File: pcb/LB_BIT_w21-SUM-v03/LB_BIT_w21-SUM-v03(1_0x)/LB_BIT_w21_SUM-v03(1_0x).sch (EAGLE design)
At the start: 24 parts

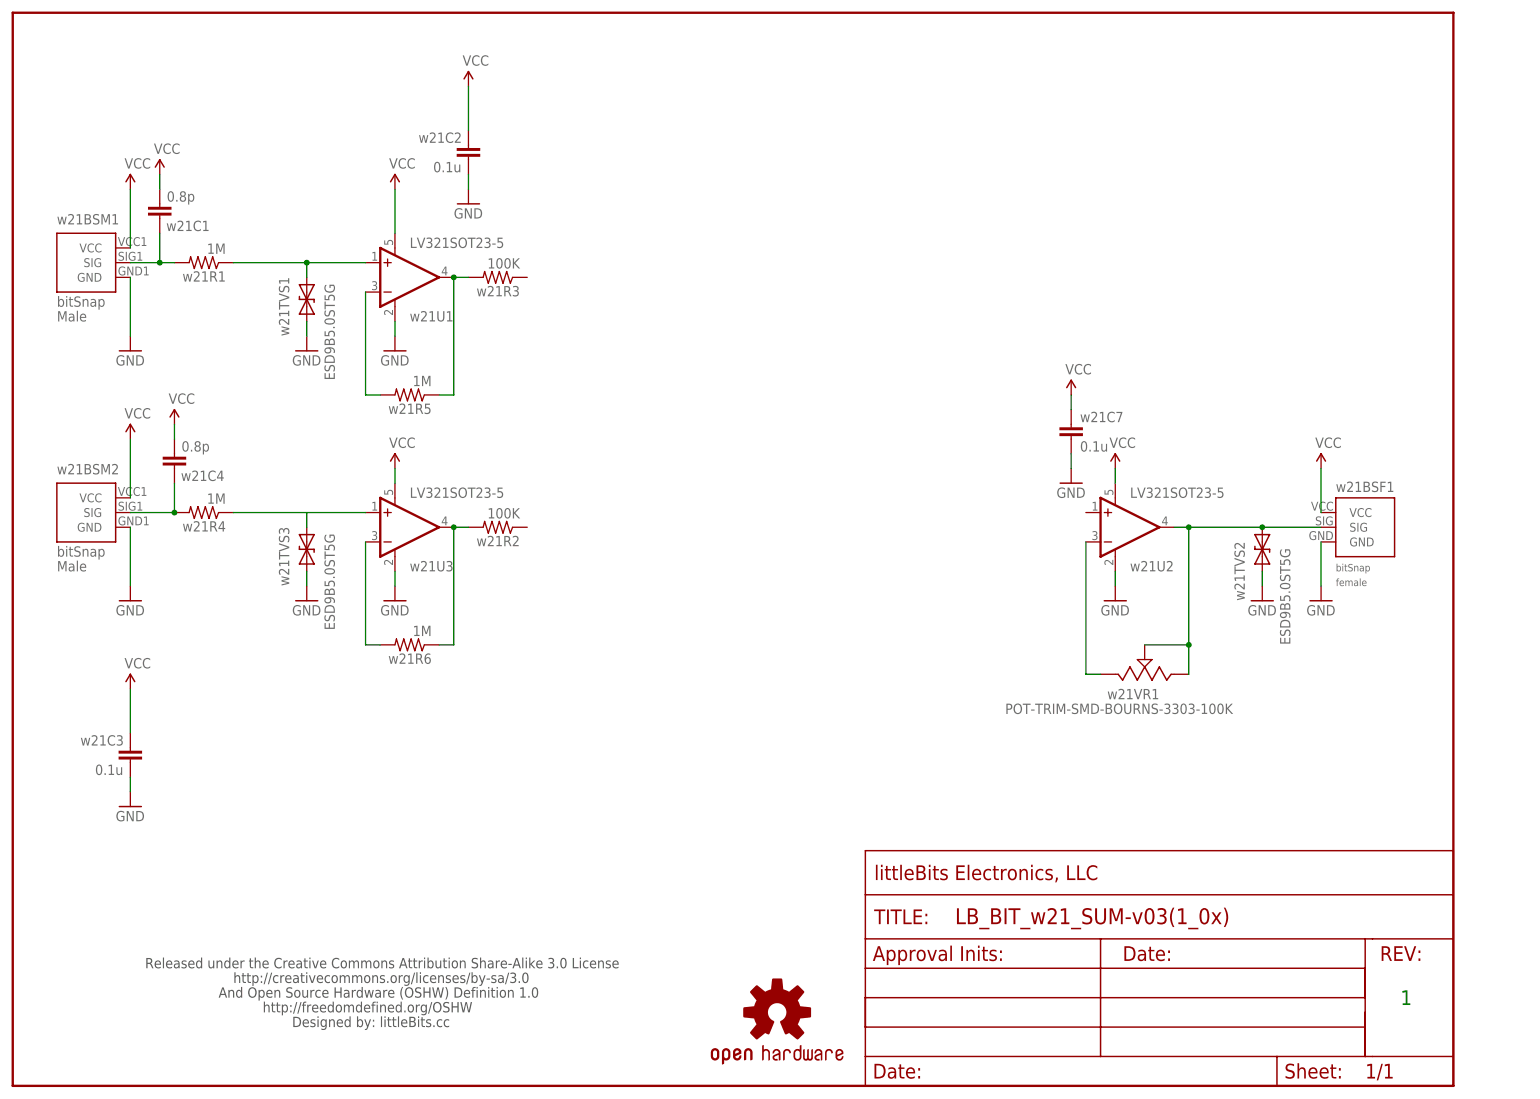
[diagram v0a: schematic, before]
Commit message: Tuned inputs and reference rail, though it may not be neccessary.  Sketched out the DC mixer and output buffer.
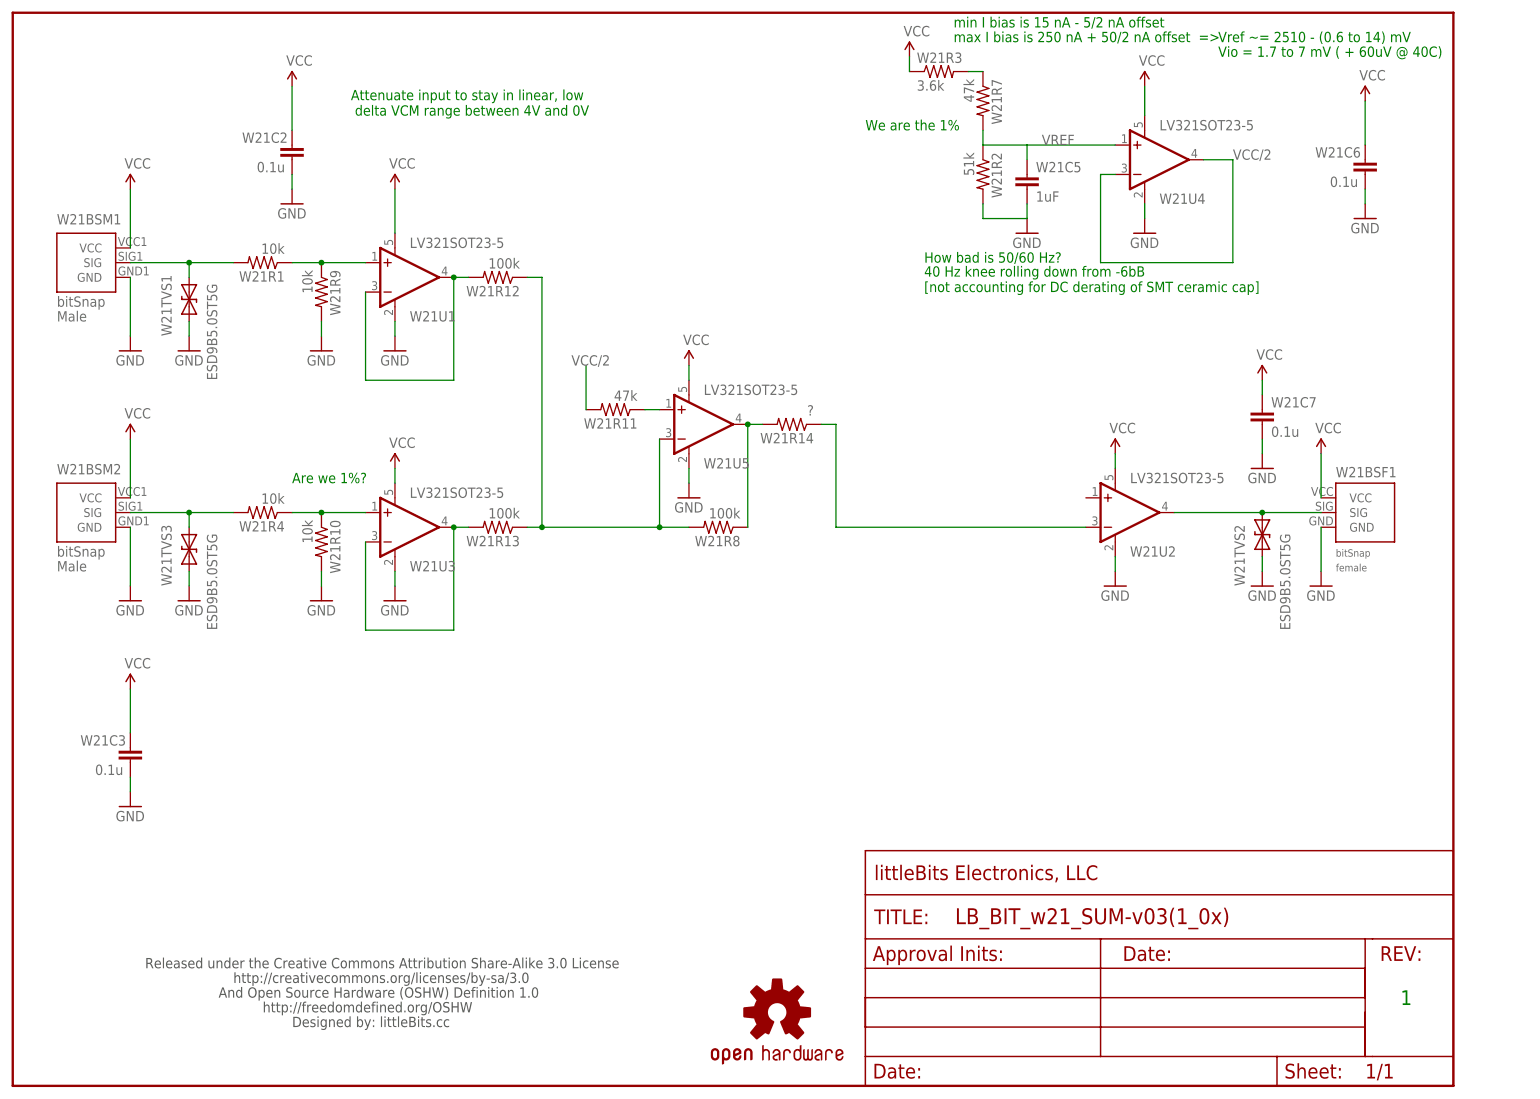
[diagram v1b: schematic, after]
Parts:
- removed w21BSF1: BITSNAP_V03_FEMALE, bitSnap:BITSNAP_V03_FEMALE
- removed w21C1, w21C4: 0.8p, LITTLEBITS:CAPCAP-0603
- removed w21C2, w21C7: 0.1u, LITTLEBITS:CAPCAP-0603
- removed w21R1, w21R4, w21R5, w21R6: 1M, LITTLEBITS:RESISTOR0603
- removed w21TVS1, w21TVS2, w21TVS3: ESD9B5.0ST5G, LITTLEBITS:DIODE-TVSSOD-923
- removed w21U2: LV321SOT23-5, LITTLEBITS:LV321SOT23-5
- removed w21VR1: POT-TRIM-SMD-BOURNS-3303-100K, LITTLEBITS:POT-TRIM-SMD-BOURNS-3303
- added W21BSF1: BITSNAP_V03_FEMALE, bitSnap:BITSNAP_V03_FEMALE
- added W21C2, W21C6, W21C7: 0.1u, LITTLEBITS:CAPCAP-0603
- added W21C5: 1uF, LITTLEBITS:CAPCAP-0603
- added W21R1, W21R10, W21R4, W21R9: 10k, LITTLEBITS:RESISTOR0603
- added W21R11, W21R7: 47k, LITTLEBITS:RESISTOR0603
- added W21R14: ?, LITTLEBITS:RESISTOR0603
- added W21R2: 51k, LITTLEBITS:RESISTOR0603
- added W21R3: 3.6k, LITTLEBITS:RESISTOR0603
- added W21R8: 100k, LITTLEBITS:RESISTOR0603
- added W21TVS1, W21TVS2, W21TVS3: ESD9B5.0ST5G, LITTLEBITS:DIODE-TVSSOD-923
- added W21U2, W21U4, W21U5: LV321SOT23-5, LITTLEBITS:LV321SOT23-5
- W21R12, W21R13: value 100K -> 100k
- renumbered w21BSM1 to W21BSM1, w21BSM2 to W21BSM2, w21C3 to W21C3, w21R2 to W21R13, w21R3 to W21R12, w21U1 to W21U1, w21U3 to W21U3
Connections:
- removed net N$4: W21R13.2, W21U3.OUT, w21R6.1
- removed net N$9: W21U1.-IN, w21R5.2
- new net N$1: W21R3.2, W21R7.1
- new net N$12: W21R12.1, W21R13.1, W21R8.2, W21U5.-IN
- new net N$13: W21R11.1, W21U5.+IN
- new net N$15: W21R14.1, W21U2.-IN
- new net VCC/2: W21R11.2, W21U4.-IN, W21U4.OUT
- new net VREF: W21C5.1, W21R2.1, W21R7.2, W21U4.+IN
- net GND: now also W21BSF1.GND, W21C2.2, W21C5.2, W21C6.2, W21C7.2, W21R10.2, W21R2.2, W21R9.2, W21TVS1.A, W21TVS2.A, W21TVS3.A, W21U2.V-, W21U4.V-, W21U5.V-; no longer w21BSF1.GND, w21C2.2, w21C7.2, w21TVS1.A, w21TVS2.A, w21TVS3.A, w21U2.V-
- net N$10: now also W21R10.1, W21R4.1; no longer w21R4.1, w21TVS3.C
- net N$11: now also W21R13.2, W21U3.OUT; no longer w21R6.2
- net N$2: now also W21R4.2, W21TVS3.C; no longer w21C4.1, w21R4.2
- net N$3: now also W21R1.1, W21R9.1; no longer w21R1.1, w21TVS1.C
- net N$5: now also W21R1.2, W21TVS1.C; no longer w21C1.1, w21R1.2
- net N$6: now also W21R14.2, W21R8.1, W21U5.OUT; no longer w21U2.-IN, w21VR1.3
- net N$7: now also W21BSF1.SIG, W21TVS2.C, W21U2.OUT; no longer w21BSF1.SIG, w21TVS2.C, w21U2.OUT, w21VR1.1, w21VR1.2
- net N$8: now also W21U1.-IN; no longer w21R5.1
- net VCC: now also W21BSF1.VCC, W21C2.1, W21C6.1, W21C7.1, W21R3.1, W21U2.V+, W21U4.V+, W21U5.V+; no longer w21BSF1.VCC, w21C1.2, w21C2.1, w21C4.2, w21C7.1, w21U2.V+
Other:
- note added: "40 Hz knee rolling down from -6bB [not accounting for DC derating of SMT ceramic cap]"
- note added: "Are we 1%?"
- note added: "Attenuate input to stay in linear, low delta VCM range between 4V and 0V"
- note added: "How bad is 50/60 Hz?"
- note added: "TODO"
- note added: "Vio = 1.7 to 7 mV ( + 60uV @ 40C)"
- note added: "Vref ~= 2510 - (0.6 to 14) mV"
- note added: "We are the 1%"
- note added: "max I bias is 250 nA + 50/2 nA offset =>"
- note added: "min I bias is 15 nA - 5/2 nA offset"

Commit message: Actual circuit prototyped and revised.
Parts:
- removed W21C5: 1uF, LITTLEBITS:CAPCAP-0603
- removed W21C6: 0.1u, LITTLEBITS:CAPCAP-0603
- removed W21R12: 100k, LITTLEBITS:RESISTOR0603
- removed W21R14: ?, LITTLEBITS:RESISTOR0603
- removed W21R2: 51k, LITTLEBITS:RESISTOR0603
- removed W21R3: 3.6k, LITTLEBITS:RESISTOR0603
- removed W21R7: 47k, LITTLEBITS:RESISTOR0603
- removed W21U2, W21U4: LV321SOT23-5, LITTLEBITS:LV321SOT23-5
- added W21R5: 51k, LITTLEBITS:RESISTOR0603
- W21R1, W21R10, W21R4, W21R9: value 10k -> 51k
- W21R13: value 100k -> 51k
- W21R6: value 47k -> 51k
- W21R8: value 100k -> 150k
- renumbered W21R11 to W21R6
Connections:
- removed net N$1: W21R3.2, W21R7.1
- removed net N$13: W21R6.1, W21U5.+IN
- removed net N$15: W21R14.1, W21U2.-IN
- removed net N$7: W21BSF1.SIG, W21TVS2.C, W21U2.OUT
- removed net VCC/2: W21R6.2, W21U4.-IN, W21U4.OUT
- removed net VREF: W21C5.1, W21R2.1, W21R7.2, W21U4.+IN
- new net N$4: W21R5.1, W21R6.1, W21U5.+IN
- net GND: now also W21R13.2; no longer W21C5.2, W21C6.2, W21R2.2, W21U2.V-, W21U4.V-
- net N$11: now also W21R6.2; no longer W21R13.2
- net N$12: no longer W21R12.1
- net N$6: now also W21BSF1.SIG, W21TVS2.C; no longer W21R14.2
- net N$8: now also W21R5.2; no longer W21R12.2
- net VCC: no longer W21C6.1, W21R3.1, W21U2.V+, W21U4.V+
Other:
- note removed: "40 Hz knee rolling down from -6bB [not accounting for DC derating of SMT ceramic cap]"
- note removed: "Are we 1%?"
- note removed: "Attenuate input to stay in linear, low delta VCM range between 4V and 0V"
- note removed: "How bad is 50/60 Hz?"
- note removed: "TODO"
- note removed: "Vio = 1.7 to 7 mV ( + 60uV @ 40C)"
- note removed: "Vref ~= 2510 - (0.6 to 14) mV"
- note removed: "max I bias is 250 nA + 50/2 nA offset =>"
- note removed: "min I bias is 15 nA - 5/2 nA offset"
- moved on the sheet: W21BSF1, W21C7, W21R13, W21TVS2
